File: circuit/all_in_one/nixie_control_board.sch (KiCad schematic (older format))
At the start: 1 part, among them CON1 BARREL_JACK

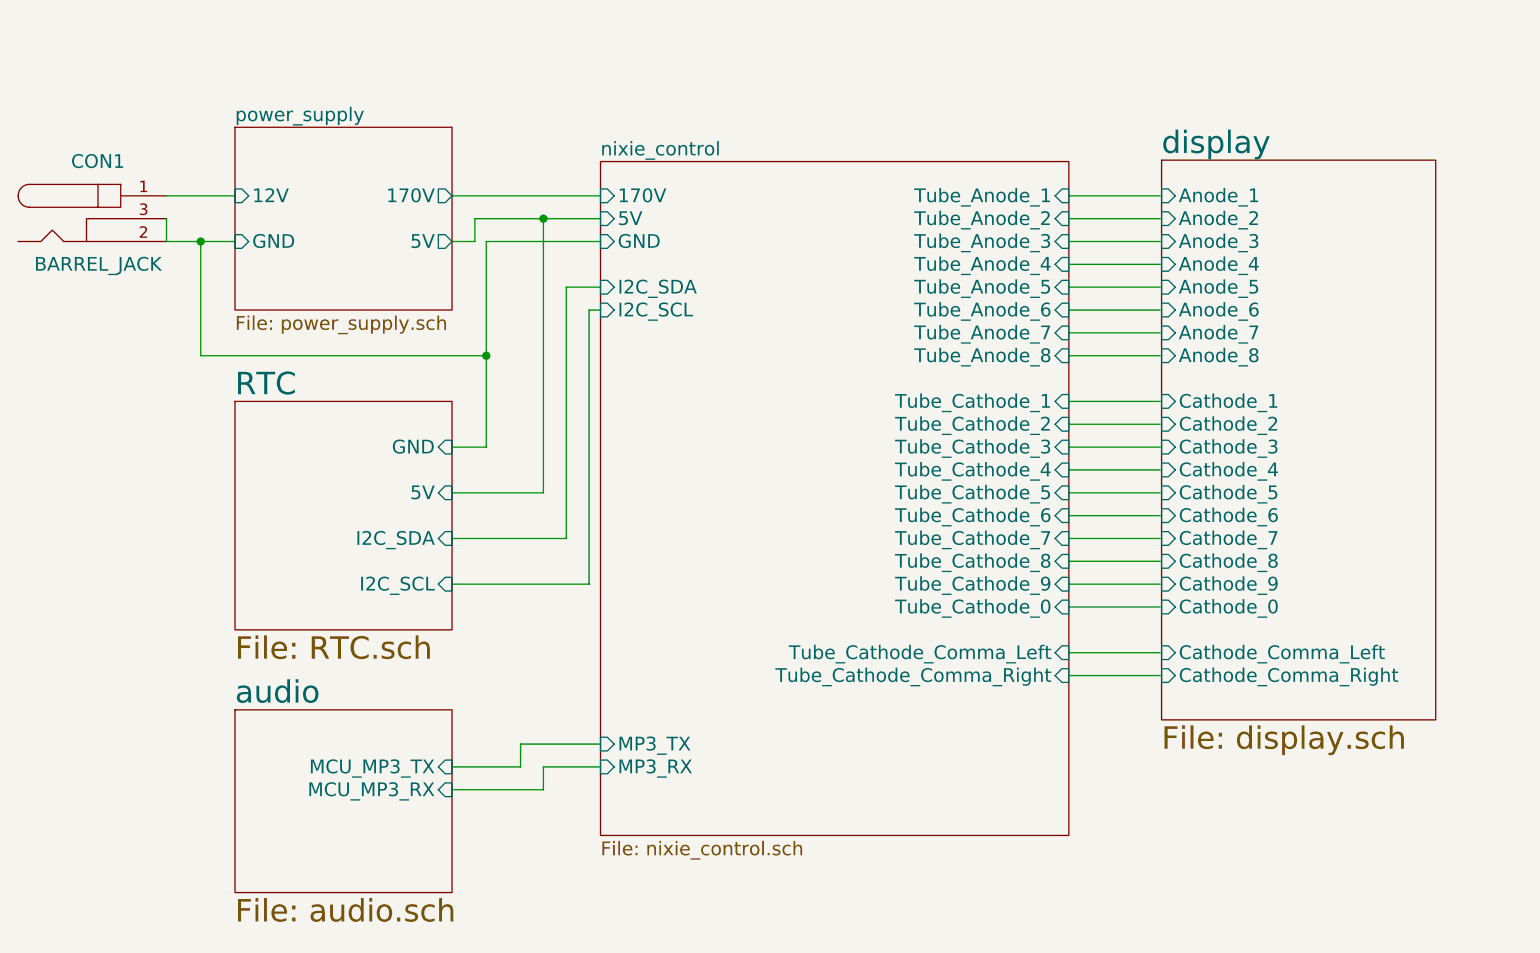
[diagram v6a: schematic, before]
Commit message: Finsihed placing all the components
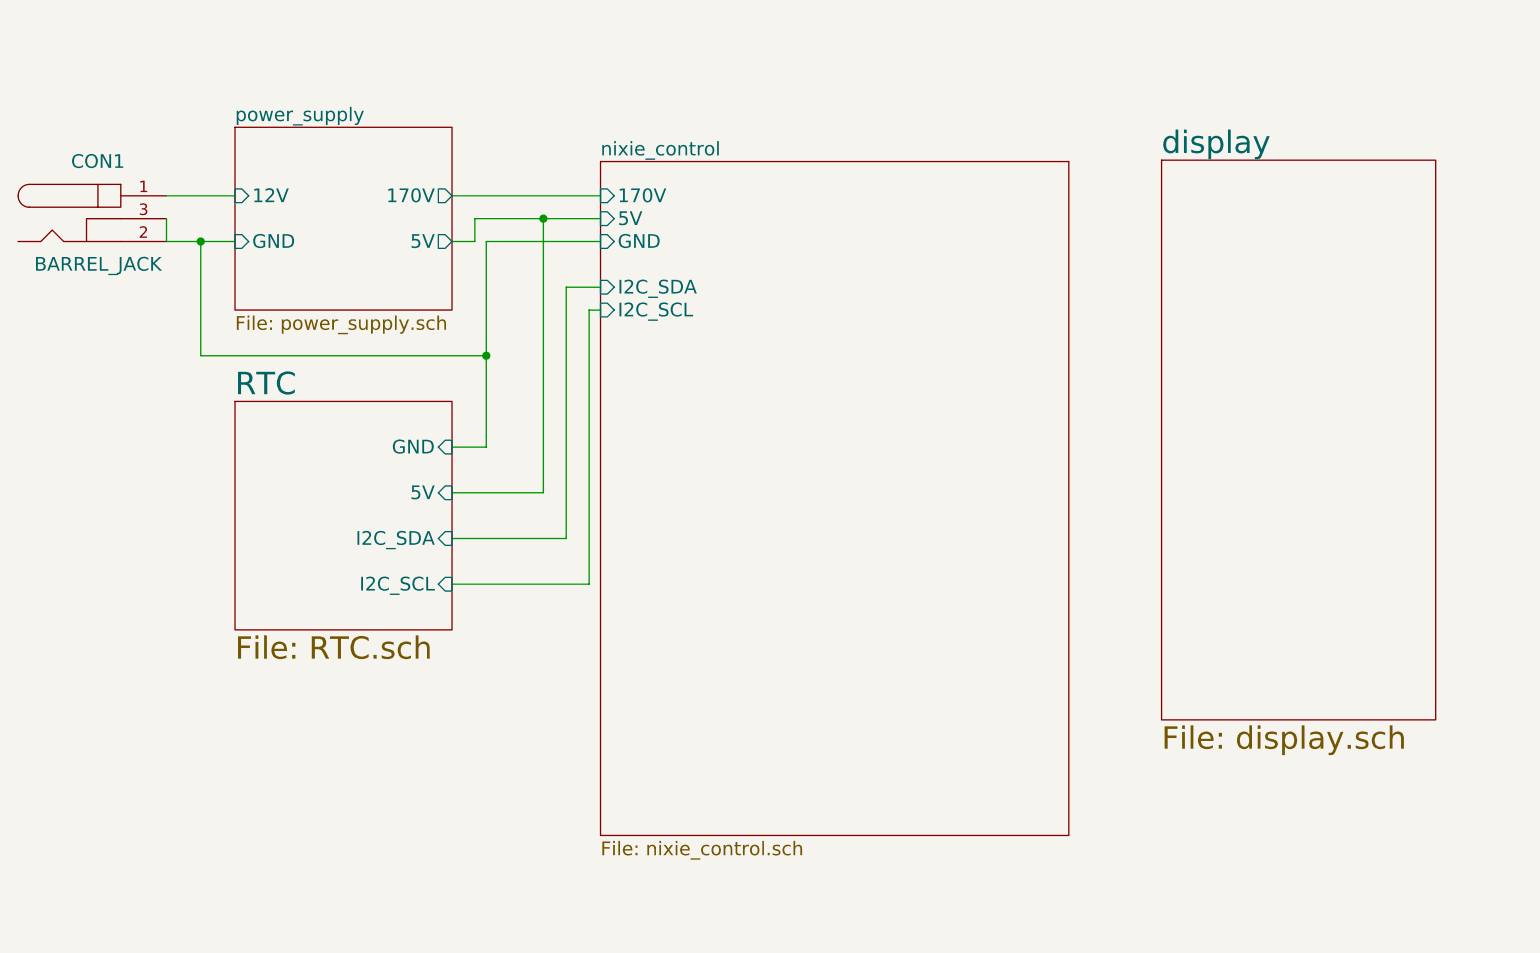
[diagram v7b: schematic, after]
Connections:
- wire segments 46 -> 20
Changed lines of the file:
@@
 $Descr A4 11693 8268
 encoding utf-8
-Sheet 1 6
+Sheet 1 5
 Title ""
 Date ""
@@
 F5 "I2C_SCL" I L 4850 3200 60
 F6 "I2C_SDA" I L 4850 3100 60
-F7 "Tube_Anode_1" I R 6900 2700 60
-F8 "Tube_Anode_2" I R 6900 2800 60
-F9 "Tube_Anode_3" I R 6900 2900 60
-F10 "Tube_Anode_4" I R 6900 3000 60
-F11 "Tube_Anode_5" I R 6900 3100 60
-F12 "Tube_Anode_6" I R 6900 3200 60
-F13 "Tube_Anode_7" I R 6900 3300 60
-F14 "Tube_Anode_8" I R 6900 3400 60
-F15 "Tube_Cathode_0" I R 6900 4500 60
-F16 "Tube_Cathode_1" I R 6900 3600 60
-F17 "Tube_Cathode_2" I R 6900 3700 60
-F18 "Tube_Cathode_3" I R 6900 3800 60
-F19 "Tube_Cathode_4" I R 6900 3900 60
-F20 "Tube_Cathode_5" I R 6900 4000 60
-F21 "Tube_Cathode_6" I R 6900 4100 60
-F22 "Tube_Cathode_7" I R 6900 4200 60
-F23 "Tube_Cathode_8" I R 6900 4300 60
-F24 "Tube_Cathode_9" I R 6900 4400 60
-F25 "Tube_Cathode_Comma_Left" I R 6900 4700 60
-F26 "Tube_Cathode_Comma_Right" I R 6900 4800 60
-F27 "MP3_TX" I L 4850 5100 60
-F28 "MP3_RX" I L 4850 5200 60
 $EndSheet
 $Sheet
@@
 $EndSheet
 $Sheet
-S 3250 4950 950  800
-U 5646A864
-F0 "audio" 98
-F1 "audio.sch" 98
-F2 "MCU_MP3_TX" I R 4200 5200 60
-F3 "MCU_MP3_RX" I R 4200 5300 60
-$EndSheet
-$Sheet
 S 7306 2544 1200 2450
 U 5646AE2C
 F0 "display" 98
 F1 "display.sch" 98
-F2 "Anode_2" I L 7306 2800 60
-F3 "Anode_1" I L 7306 2700 60
-F4 "Anode_3" I L 7306 2900 60
-F5 "Anode_4" I L 7306 3000 60
-F6 "Anode_5" I L 7306 3100 60
-F7 "Anode_6" I L 7306 3200 60
-F8 "Anode_7" I L 7306 3300 60
-F9 "Anode_8" I L 7306 3400 60
-F10 "Cathode_4" I L 7306 3900 60
-F11 "Cathode_3" I L 7306 3800 60
-F12 "Cathode_2" I L 7306 3700 60
-F13 "Cathode_1" I L 7306 3600 60
-F14 "Cathode_Comma_Right" I L 7306 4800 60
-F15 "Cathode_Comma_Left" I L 7306 4700 60
-F16 "Cathode_5" I L 7306 4000 60
-F17 "Cathode_6" I L 7306 4100 60
-F18 "Cathode_7" I L 7306 4200 60
-F19 "Cathode_8" I L 7306 4300 60
-F20 "Cathode_9" I L 7306 4400 60
-F21 "Cathode_0" I L 7306 4500 60
 $EndSheet
 $Comp
@@
 Wire Wire Line
 	3100 2900 3100 3400
-Wire Wire Line
-	7300 2700 6900 2700
-Wire Wire Line
-	7300 2800 6900 2800
-Wire Wire Line
-	7300 2900 6900 2900
-Wire Wire Line
-	7300 3000 6900 3000
-Wire Wire Line
-	7300 3100 6900 3100
-Wire Wire Line
-	7300 3200 6900 3200
-Wire Wire Line
-	7300 3300 6900 3300
-Wire Wire Line
-	7300 3400 6900 3400
-Wire Wire Line
-	7300 3600 6900 3600
-Wire Wire Line
-	7300 3700 6900 3700
-Wire Wire Line
-	7300 3800 6900 3800
-Wire Wire Line
-	6900 3900 7300 3900
-Wire Wire Line
-	7300 4000 6900 4000
-Wire Wire Line
-	7300 4100 6900 4100
-Wire Wire Line
-	7300 4200 6900 4200
-Wire Wire Line
-	7300 4300 6900 4300
-Wire Wire Line
-	7300 4400 6900 4400
-Wire Wire Line
-	7300 4500 6900 4500
 Wire Wire Line
 	4200 2700 4850 2700
@@
 	4800 4400 4200 4400
 Wire Wire Line
-	7300 4700 6900 4700
-Wire Wire Line
-	7300 4800 6900 4800
-Wire Wire Line
-	4200 5200 4500 5200
-Wire Wire Line
-	4500 5200 4500 5100
-Wire Wire Line
-	4500 5100 4850 5100
-Wire Wire Line
-	4200 5300 4600 5300
-Wire Wire Line
-	4600 5300 4600 5200
-Wire Wire Line
-	4600 5200 4850 5200
-Wire Wire Line
 	2950 2800 2950 2900

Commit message: New hardware is almost finished
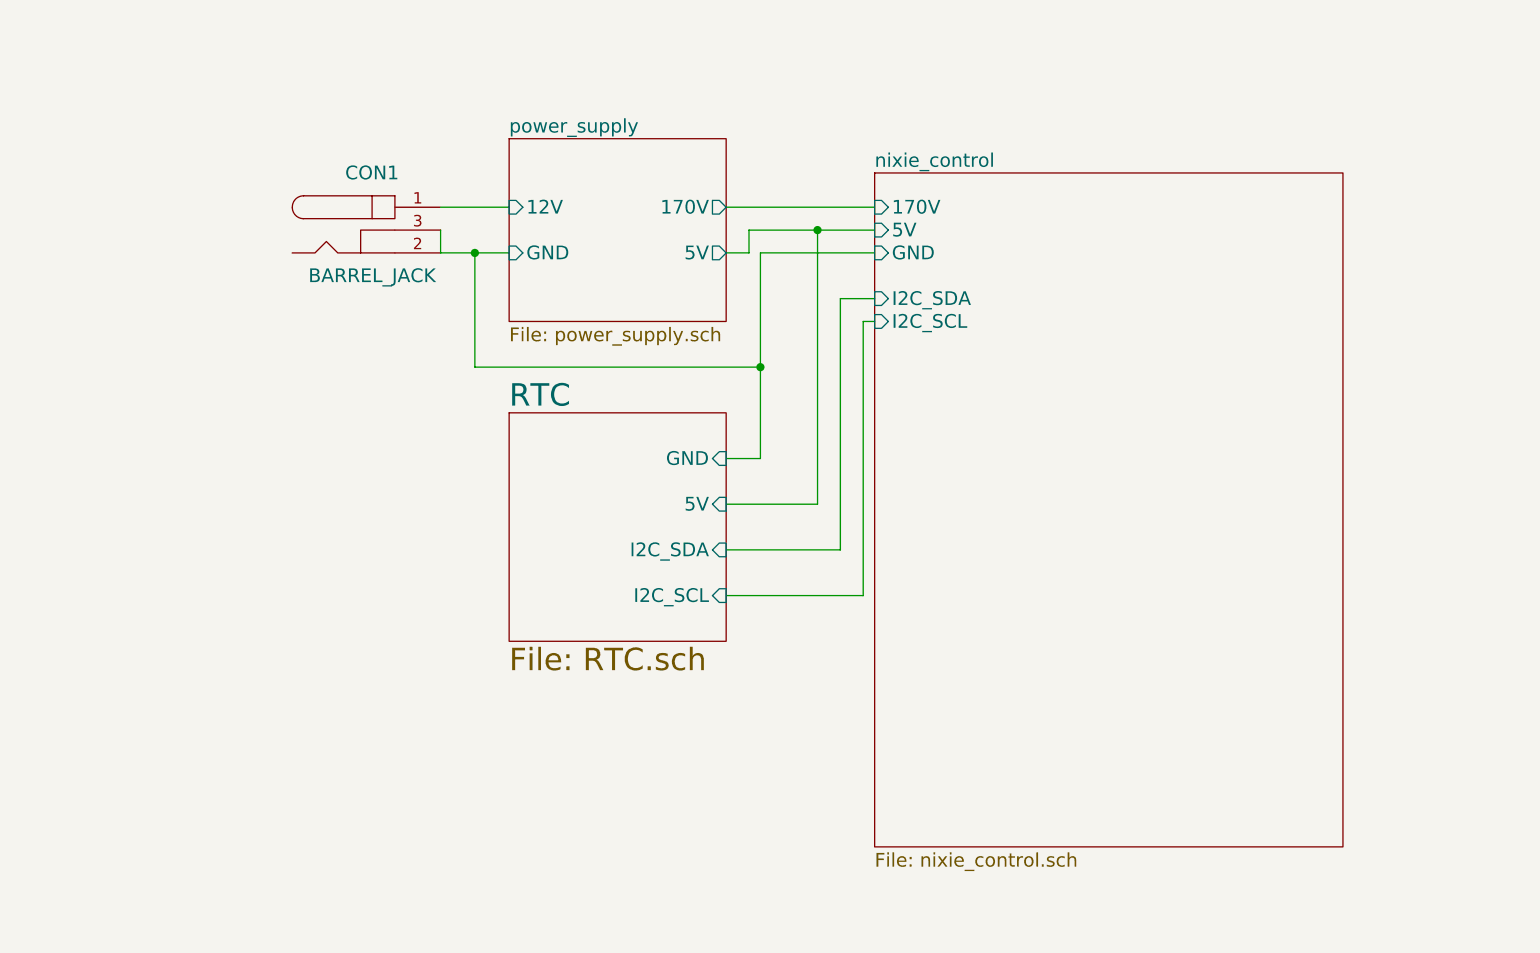
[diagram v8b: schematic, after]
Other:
- moved on the sheet: CON1
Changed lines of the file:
@@
 $Descr A4 11693 8268
 encoding utf-8
-Sheet 1 5
+Sheet 1 4
 Title ""
 Date ""
@@
 $EndDescr
 $Sheet
-S 3250 2400 950  800
+S 4450 2450 950  800
 U 5645F24C
 F0 "power_supply" 60
 F1 "power_supply.sch" 60
-F2 "170V" O R 4200 2700 60
-F3 "5V" O R 4200 2900 60
-F4 "12V" I L 3250 2700 60
-F5 "GND" I L 3250 2900 60
+F2 "170V" O R 5400 2750 60
+F3 "5V" O R 5400 2950 60
+F4 "12V" I L 4450 2750 60
+F5 "GND" I L 4450 2950 60
 $EndSheet
 $Sheet
-S 4850 2550 2050 2950
+S 6050 2600 2050 2950
 U 5645F2A4
 F0 "nixie_control" 60
 F1 "nixie_control.sch" 60
-F2 "170V" I L 4850 2700 60
-F3 "5V" I L 4850 2800 60
-F4 "GND" I L 4850 2900 60
-F5 "I2C_SCL" I L 4850 3200 60
-F6 "I2C_SDA" I L 4850 3100 60
+F2 "170V" I L 6050 2750 60
+F3 "5V" I L 6050 2850 60
+F4 "GND" I L 6050 2950 60
+F5 "I2C_SCL" I L 6050 3250 60
+F6 "I2C_SDA" I L 6050 3150 60
 $EndSheet
 $Sheet
-S 3250 3600 950  1000
+S 4450 3650 950  1000
 U 5646A754
 F0 "RTC" 98
 F1 "RTC.sch" 98
-F2 "I2C_SCL" I R 4200 4400 60
-F3 "I2C_SDA" I R 4200 4200 60
-F4 "5V" I R 4200 4000 60
-F5 "GND" I R 4200 3800 60
-$EndSheet
-$Sheet
-S 7306 2544 1200 2450
-U 5646AE2C
-F0 "display" 98
-F1 "display.sch" 98
+F2 "I2C_SCL" I R 5400 4450 60
+F3 "I2C_SDA" I R 5400 4250 60
+F4 "5V" I R 5400 4050 60
+F5 "GND" I R 5400 3850 60
 $EndSheet
 $Comp
 L BARREL_JACK CON1
 U 1 1 5657C68E
-P 2650 2800
-F 0 "CON1" H 2650 3050 60  0000 C CNN
-F 1 "BARREL_JACK" H 2650 2600 60  0000 C CNN
-F 2 "Connect:JACK_ALIM" H 2650 2800 60  0001 C CNN
-F 3 "" H 2650 2800 60  0000 C CNN
-	1    2650 2800
+P 3850 2850
+F 0 "CON1" H 3850 3100 60  0000 C CNN
+F 1 "BARREL_JACK" H 3850 2650 60  0000 C CNN
+F 2 "Connect:JACK_ALIM" H 3850 2850 60  0001 C CNN
+F 3 "" H 3850 2850 60  0000 C CNN
+	1    3850 2850
 	1    0    0    -1
 $EndComp
 Wire Wire Line
-	2950 2700 3250 2700
+	4150 2750 4450 2750
 Wire Wire Line
-	2950 2900 3250 2900
+	4150 2950 4450 2950
 Wire Wire Line
-	3100 2900 3100 3400
+	4300 2950 4300 3450
 Wire Wire Line
-	4200 2700 4850 2700
+	5400 2750 6050 2750
 Wire Wire Line
-	4200 2900 4300 2900
+	5400 2950 5500 2950
 Wire Wire Line
-	4300 2900 4300 2800
+	5500 2950 5500 2850
 Wire Wire Line
-	4300 2800 4850 2800
+	5500 2850 6050 2850
 Wire Wire Line
-	3100 3400 4350 3400
+	4300 3450 5550 3450
 Wire Wire Line
-	4350 2900 4350 3800
+	5550 2950 5550 3850
 Wire Wire Line
-	4350 2900 4850 2900
-Connection ~ 3100 2900
+	5550 2950 6050 2950
+Connection ~ 4300 2950
 Wire Wire Line
-	4600 2800 4600 4000
+	5800 2850 5800 4050
 Wire Wire Line
-	4600 4000 4200 4000
-Connection ~ 4600 2800
+	5800 4050 5400 4050
+Connection ~ 5800 2850
 Wire Wire Line
-	4350 3800 4200 3800
-Connection ~ 4350 3400
+	5550 3850 5400 3850
+Connection ~ 5550 3450
 Wire Wire Line
-	4200 4200 4700 4200
+	5400 4250 5900 4250
 Wire Wire Line
-	4700 4200 4700 3100
+	5900 4250 5900 3150
 Wire Wire Line
-	4700 3100 4850 3100
+	5900 3150 6050 3150
 Wire Wire Line
-	4850 3200 4800 3200
+	6050 3250 6000 3250
 Wire Wire Line
-	4800 3200 4800 4400
+	6000 3250 6000 4450
 Wire Wire Line
-	4800 4400 4200 4400
+	6000 4450 5400 4450
 Wire Wire Line
-	2950 2800 2950 2900
+	4150 2850 4150 2950
 $EndSCHEMATC
